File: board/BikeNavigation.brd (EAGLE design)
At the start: 38.9 x 48.9 mm, 104 parts, among them IC1 STP16CP05, IC5 ATMEGA32U4TQFP-44, IC6 LTC2950CDDB-1, J1 MICRO-USB-SMD(ZX62-B-5PA), SW1 436331045822, U1 MCP1824-3.3V (fixed), U2 MCP73831, Y2 16Mhz

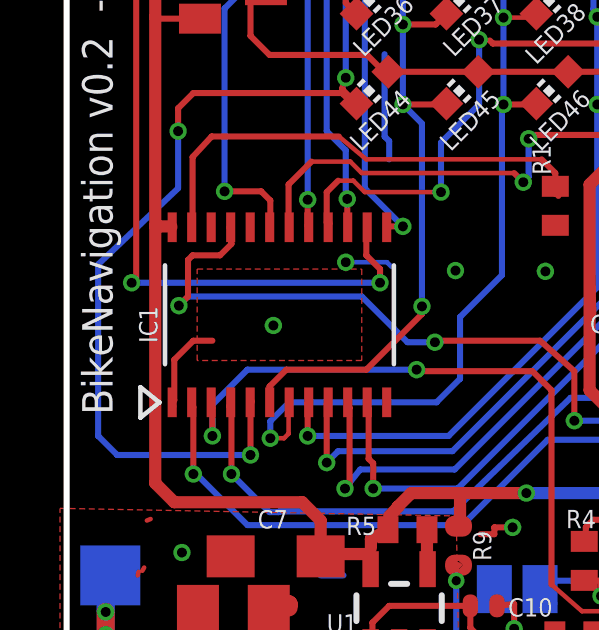
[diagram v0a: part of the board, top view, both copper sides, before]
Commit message: Fix the LED driver IC designation in the board file
Change it to correct "IC2" instead of incorrect and
duplicate "IC1". Thanks to @dwlocks for reporting.

Closes: #2
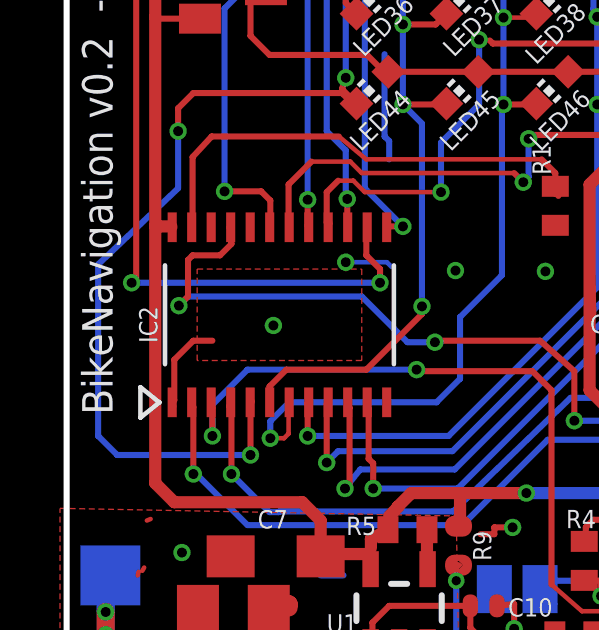
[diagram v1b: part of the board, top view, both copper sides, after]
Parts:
- added IC2: STP16CP05, BikeNavigation:TSSOP24
- IC1: value STP16CP05 -> HMC5883LSMD; device BikeNavigation:TSSOP24 -> SparkFun-Sensors:16LPCC
- moved IC1 14.5 mm to (21.8, 21.5)
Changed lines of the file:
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@@
 <attribute name="VALUE" x="12.2174" y="15.9258" size="1.27" layer="27" rot="R180"/>
 </element>
-<element name="IC1" library="BikeNavigation" package="TSSOP24" value="STP16CP05" x="7.3152" y="21.1836" smashed="yes">
+<element name="IC2" library="BikeNavigation" package="TSSOP24" value="STP16CP05" x="7.3152" y="21.1836" smashed="yes">
 <attribute name="NAME" x="3.2466" y="20.2438" size="0.6096" layer="25" font="vector" ratio="9" rot="R90"/>
 <attribute name="VALUE" x="12.5014" y="19.1008" size="1.27" layer="27" font="vector" ratio="9" rot="R90"/>
